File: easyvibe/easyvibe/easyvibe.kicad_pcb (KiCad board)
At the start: 2 copper layers, 109.5 x 54 mm, 79 parts, among them U1 TL062, U2 TL062, U3 TL062, U4 TL062

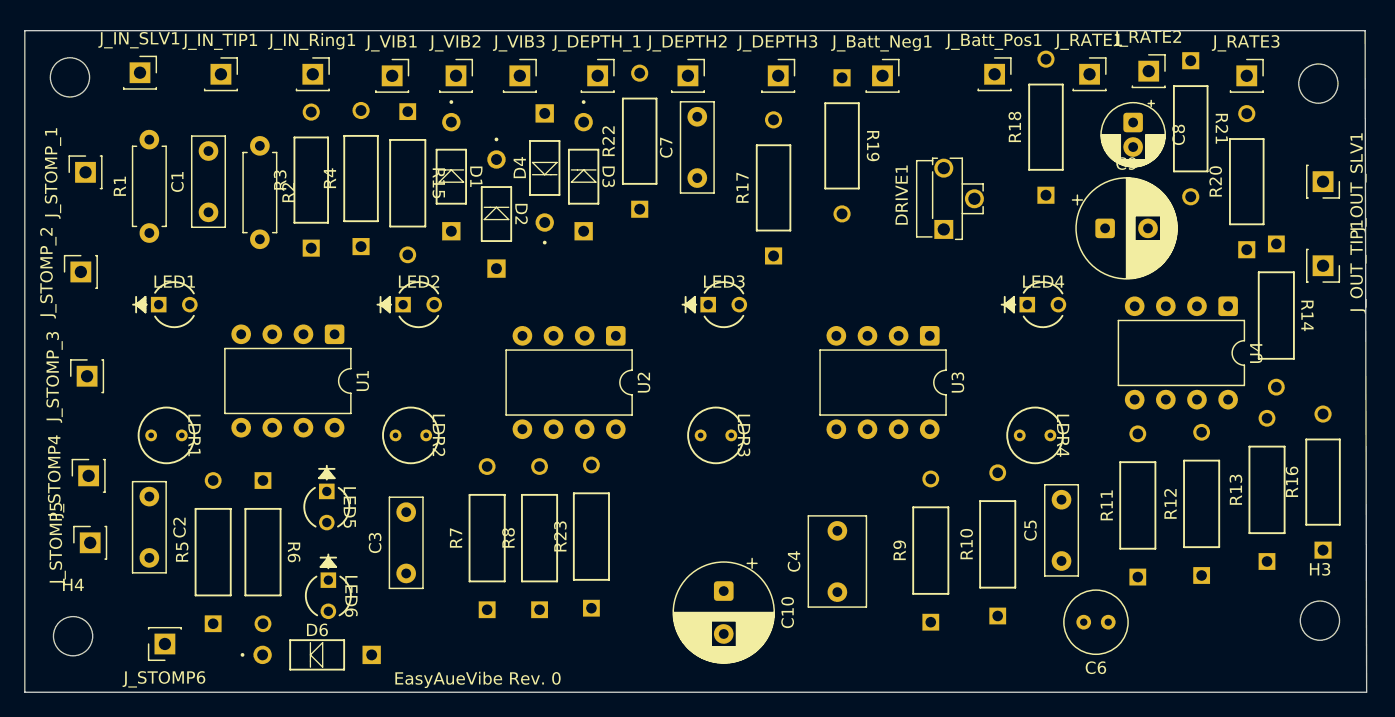
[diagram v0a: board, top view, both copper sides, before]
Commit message: autorouted version sent to oshpark
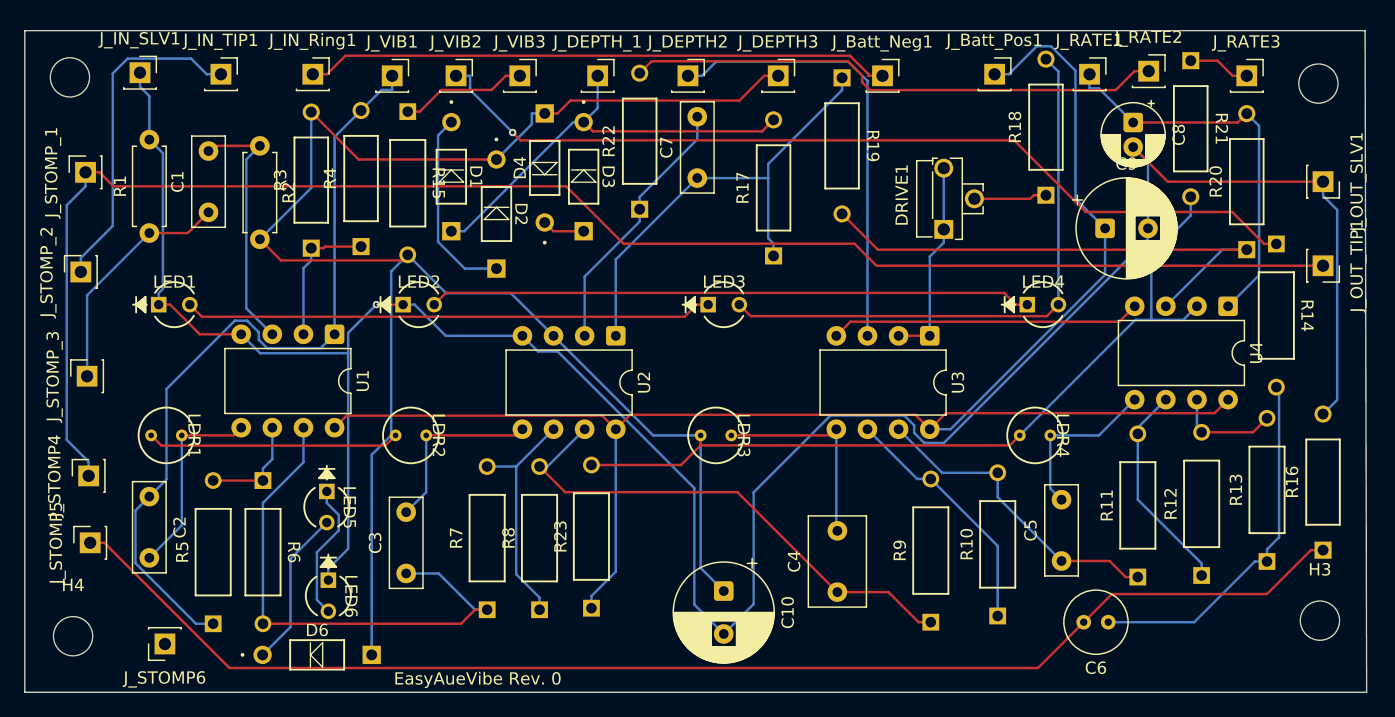
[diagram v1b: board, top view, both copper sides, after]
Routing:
- net Net-(D2-K): track 0.00 -> 233.4 mm
- net GND: track 0.00 -> 206.2 mm, vias 0 -> 1
- net +9V: track 0.00 -> 136.7 mm
- net Net-(J_OUT_TIP1-Pin_1): track 0.00 -> 130.3 mm
- net Net-(J_STOMP5-Pin_1): track 0.00 -> 108.8 mm
- net Net-(J_VIB2-Pin_1): track 0.00 -> 73.3 mm, vias 0 -> 1
- net Net-(J_VIB1-Pin_1): track 0.00 -> 65.0 mm
- net Net-(LED2-A): track 0.00 -> 49.2 mm
- net Net-(J_Batt_Neg1-Pin_1): track 0.00 -> 47.9 mm
- net Net-(LED3-A): track 0.00 -> 47.3 mm
- net Net-(C3-Pad1): track 0.00 -> 44.0 mm
- net Net-(J_RATE2-Pin_1): track 0.00 -> 43.9 mm
- net Net-(LED1-A): track 0.00 -> 43.1 mm
- net Net-(U4A-+): track 0.00 -> 42.7 mm
- net Net-(C4-Pad1): track 0.00 -> 42.1 mm
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
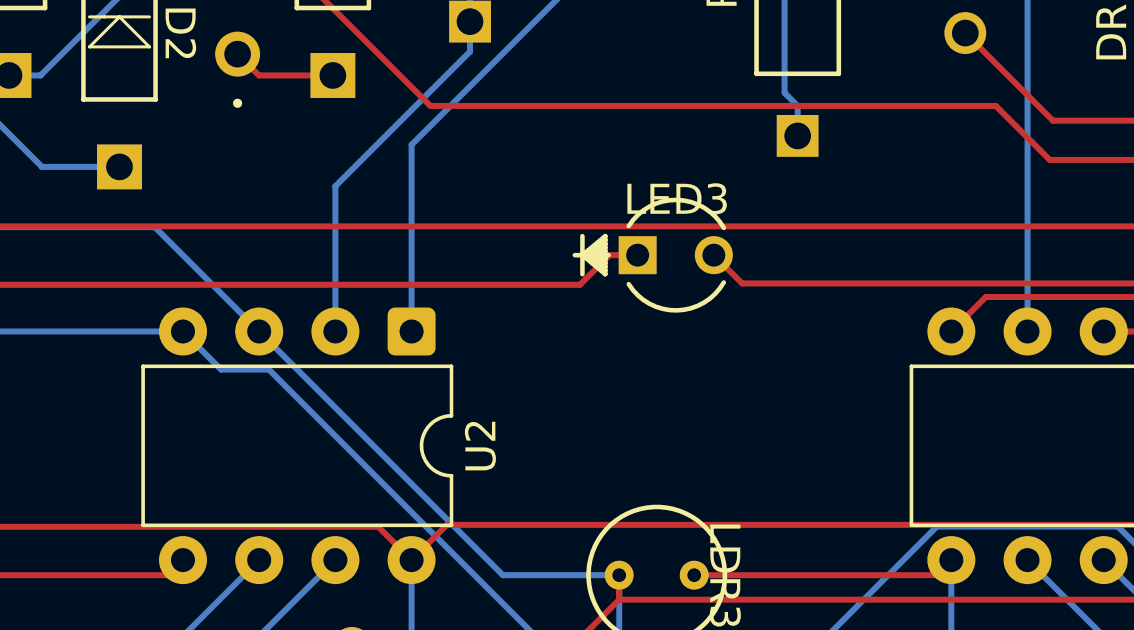
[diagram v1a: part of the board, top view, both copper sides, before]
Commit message: Fix switch wiring
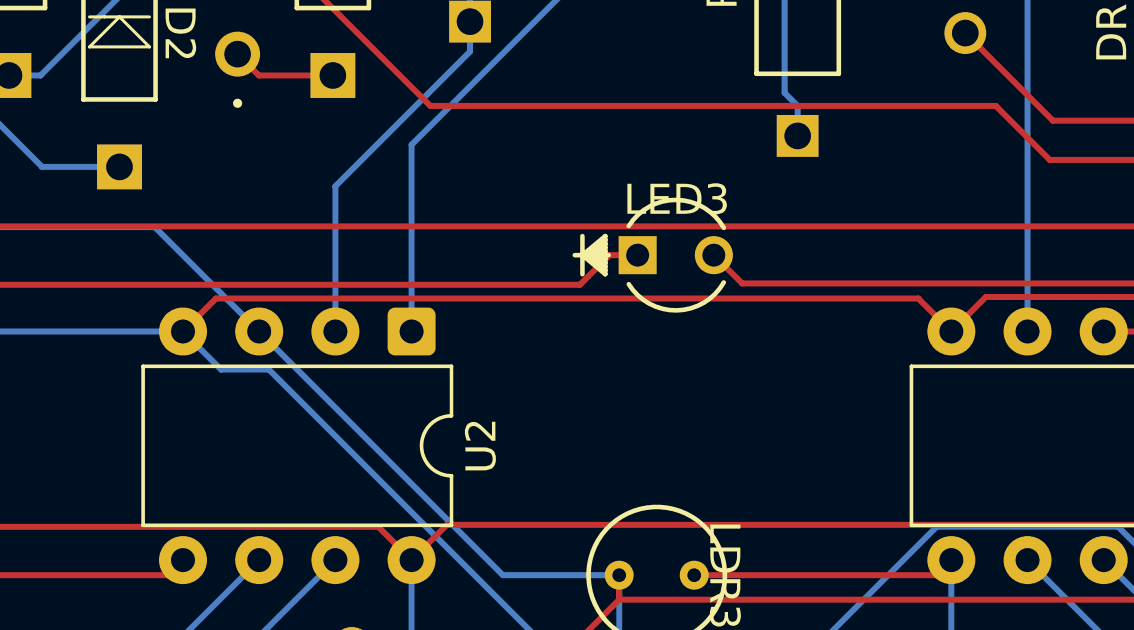
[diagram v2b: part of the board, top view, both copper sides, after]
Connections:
- U3 pad 4: Net-(U3C-V-) -> GND
- U4 pad 4: Net-(U3C-V-) -> GND
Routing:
- net GND: track 206.2 -> 258.0 mm
- net Net-(U3C-V-): track 25.3 -> 0.00 mm
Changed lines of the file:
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@@
 			(layers "*.Cu" "*.Mask")
 			(remove_unused_layers no)
-			(net "Net-(U3C-V-)")
+			(net "GND")
 			(pinfunction "V-_4")
 			(pintype "power_in")
@@
 		(sheetname "/")
 		(sheetfile "easyvibe.kicad_sch")
+		(units
+			(unit
+				(name "A")
+				(pins)
+			)
+		)
 		(attr exclude_from_bom)
 		(duplicate_pad_numbers_are_jumpers no)
@@
 			(layers "*.Cu" "*.Mask")
 			(remove_unused_layers no)
-			(net "Net-(U3C-V-)")
+			(net "GND")
 			(pinfunction "V-_4")
 			(pintype "power_in")
@@
 		(sheetname "/")
 		(sheetfile "easyvibe.kicad_sch")
+		(units
+			(unit
+				(name "A")
+				(pins)
+			)
+		)
 		(attr exclude_from_bom)
 		(duplicate_pad_numbers_are_jumpers no)
@@
 	)
 	(segment
-		(start 128.278 61.973)
-		(end 106.3493 61.973)
-		(width 0.2)
-		(layer "F.Cu")
-		(net "Net-(U3C-V-)")
-	)
-	(segment
-		(start 106.3493 61.973)
-		(end 105.1983 63.124)
-		(width 0.2)
-		(layer "F.Cu")
-		(net "Net-(U3C-V-)")
-	)
-	(segment
-		(start 129.54 60.711)
-		(end 128.278 61.973)
-		(width 0.2)
-		(layer "F.Cu")
-		(net "Net-(U3C-V-)")
-	)
-	(segment
 		(start 96.627 71.247)
 		(end 104.6953 71.247)
@@
 	)
 	(segment
+		(start 128.278 61.973)
+		(end 106.3493 61.973)
+		(width 0.2)
+		(layer "F.Cu")
+		(net "GND")
+	)
+	(segment
 		(start 53.2657 62.997)
 		(end 56.642 62.997)
@@
 	)
 	(segment
+		(start 105.1983 63.124)
+		(end 104.0983 62.024)
+		(width 0.2)
+		(layer "F.Cu")
+		(net "GND")
+	)
+	(segment
+		(start 106.3493 61.973)
+		(end 105.1983 63.124)
+		(width 0.2)
+		(layer "F.Cu")
+		(net "GND")
+	)
+	(segment
+		(start 80.6867 62.024)
+		(end 79.5867 63.124)
+		(width 0.2)
+		(layer "F.Cu")
+		(net "GND")
+	)
+	(segment
 		(start 132.239 50.546)
 		(end 129.413 47.72)
 		(width 0.2)
 		(layer "F.Cu")
+		(net "GND")
+	)
+	(segment
+		(start 104.0983 62.024)
+		(end 80.6867 62.024)
+		(width 0.2)
+		(layer "F.Cu")
+		(net "GND")
+	)
+	(segment
+		(start 129.54 60.711)
+		(end 128.278 61.973)
+		(width 0.2)
+		(layer "F.Cu")
